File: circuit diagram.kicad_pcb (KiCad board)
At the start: 2 copper layers, 76.2 x 90.9 mm, 45 parts, among them J1 Conn_01x02_Pin, J2 Conn_01x04_Pin, J3 Conn_01x06_Pin, J4 Conn_01x05_Pin, SW1 Kailh Choc v1, SW2 Kailh Choc v1, SW3 Kailh Choc v1, SW4 Kailh Choc v1, SW5 Kailh Choc v1, U1 74HC595, U2 74HC595, U3 74HC595, U4 SC52-11EWA, U5 SC52-11EWA, U6 SC52-11EWA

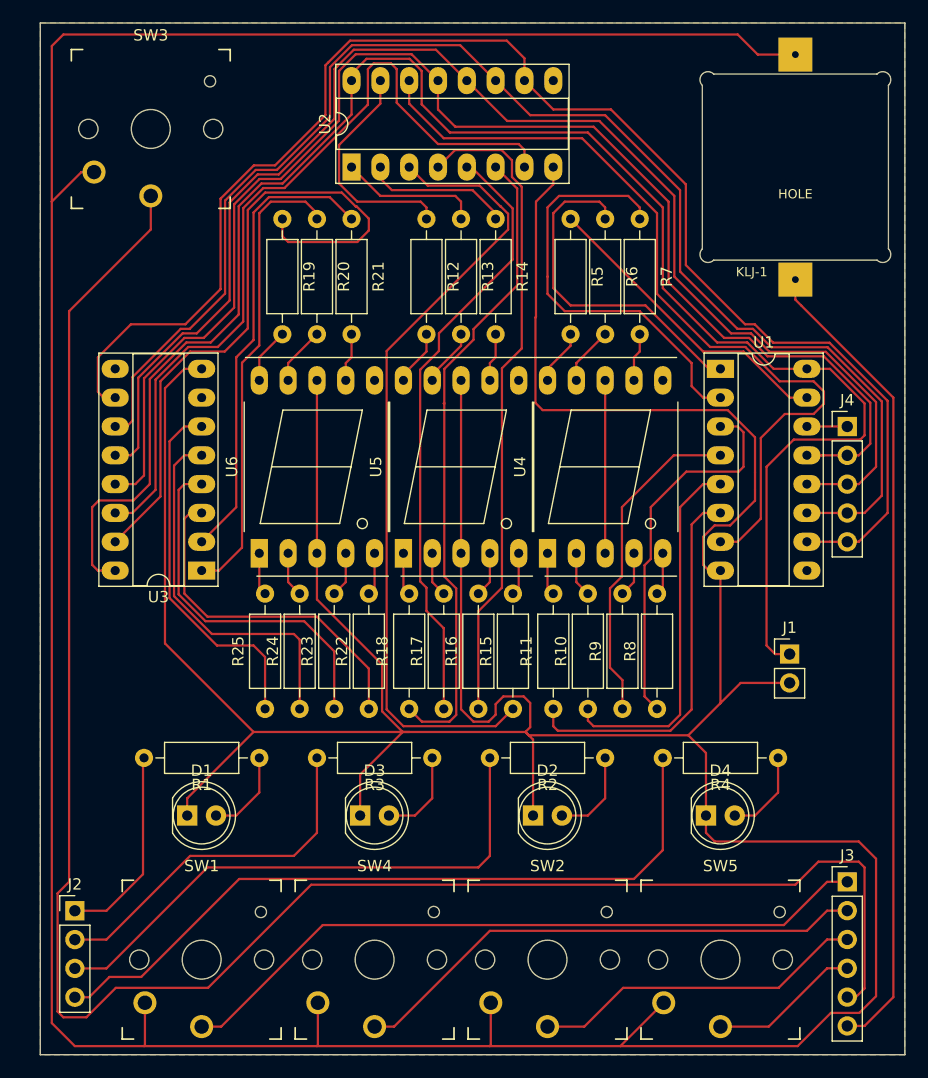
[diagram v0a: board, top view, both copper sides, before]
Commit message: Fixed key spacing and flipped components. Added gerber files.
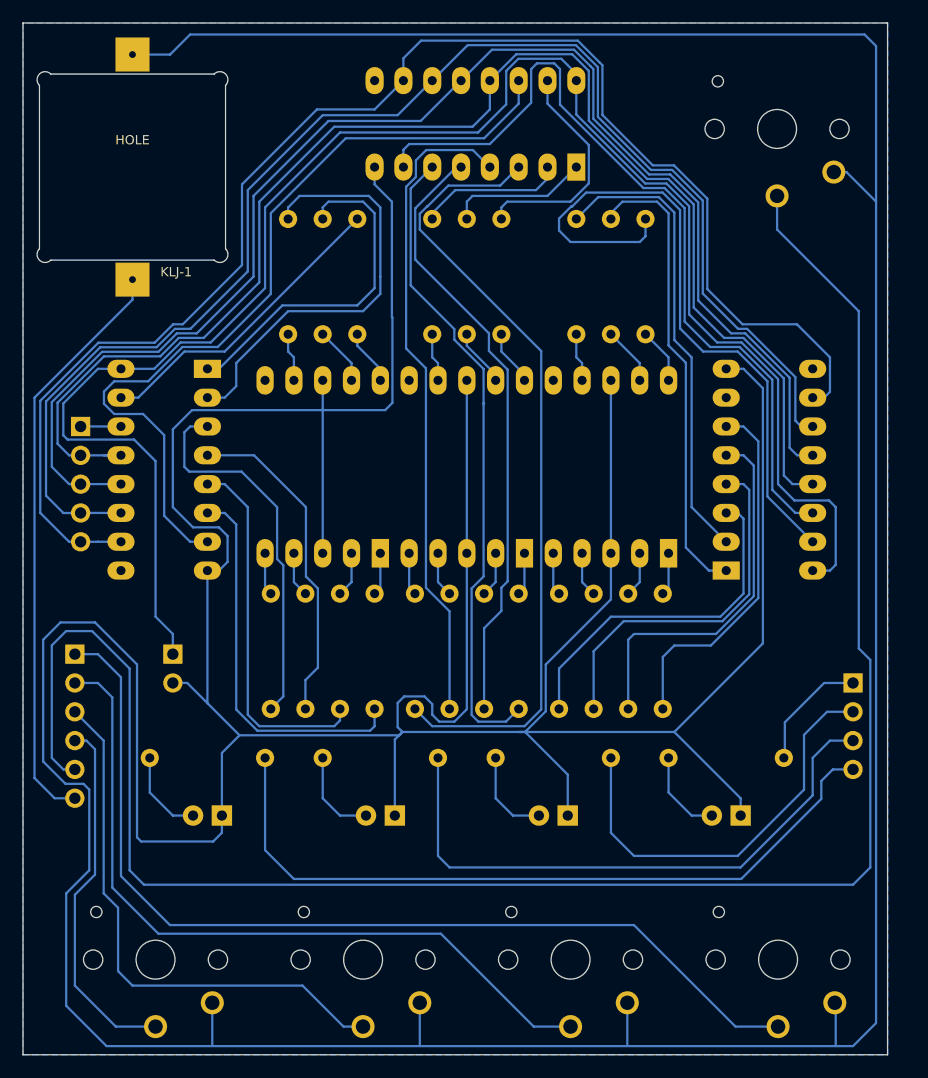
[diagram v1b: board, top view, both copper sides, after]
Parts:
- D1, D2, D3, D4, J1, J2, J3, J4, KLJ-1, R1, R10, R11, R12, R13, R14, R15, R16, R17, R18, R19, R2, R20, R21, R22, R23, R24, R25, R3, R4, R5, R6, R7, R8, R9, SW1, SW2, SW3, SW4, SW5, U1, U2, U3, U4, U5, U6: moved to B.Cu
- moved J2 71.5 mm to (101.1, 87.6), turned to 180 degrees
- moved J3 71.0 mm to (32.5, 85.1), turned to 180 degrees
- moved J4 67.6 mm to (33.0, 65.0), turned to 180 degrees
- moved KLJ-1 58.4 mm to (37.6, 42.2), turned to 0 degrees
- moved R4 55.4 mm to (39.1, 94.2), turned to 0 degrees
- moved SW3 55.2 mm to (94.4, 38.8), turned to 180 degrees
- moved J1 54.4 mm to (41.1, 85.1), turned to 180 degrees
- moved SW1 50.8 mm to (94.5, 112.0), turned to 180 degrees
- moved SW5 49.8 mm to (39.6, 112.0), turned to 180 degrees
- moved D1 48.8 mm to (91.2, 99.3), turned to 180 degrees
- moved U3 46.2 mm to (89.9, 77.7), turned to 0 degrees
- moved U1 45.2 mm to (44.2, 59.9), turned to 180 degrees
- moved D4 42.7 mm to (45.5, 99.3), turned to 180 degrees
- moved R1 36.1 mm to (84.8, 94.2), turned to 0 degrees
- moved U6 36.1 mm to (84.8, 76.2)
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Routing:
- net GND: track 559.4 -> 595.3 mm
- net /BTN_TURQ: track 62.2 -> 85.8 mm
- net /BTN_YLW: track 45.9 -> 66.1 mm
- net /BUZZER: track 71.9 -> 51.8 mm
- net /BTN_GRN: track 13.3 -> 32.3 mm
- net /BTN_RED: track 29.6 -> 48.1 mm
- net /LED_TURQ: track 17.7 -> 10.5 mm
- net /LED_YLW: track 31.8 -> 36.9 mm
- net /BTN_START: track 165.0 -> 167.9 mm
- net /LED_RED: track 49.3 -> 52.2 mm
- net VCC: track 154.0 -> 152.9 mm
- net /LED_GRN: track 65.3 -> 65.9 mm
- added copper zone on B.Cu, net GND
- removed copper zone on F.Cu, net GND
